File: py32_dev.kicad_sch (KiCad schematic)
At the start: 34 parts, among them J1 Board Pwr, J2 Conn_01x18, J3 Conn_01x18, SW1 Usr, SW2 Reset, U1 uA7805, U2 PY32F030K1xT, Y1 24MHz, Y2 32.768KHz

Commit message: Updated README
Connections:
- net GND: now also J2.1 (Pin_1); no longer J3.1 (Pin_1)
- net VDD: now also J3.1 (Pin_1); no longer J2.1 (Pin_1)
- net VBUS: now reaches C1.1, F1.1, J1.A9 (VBUS), J1.B9 (VBUS)
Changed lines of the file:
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@@
   (junction (at 57.15 60.96) (diameter 0) (color 0 0 0 0)
   )
+  (junction (at 207.01 33.02) (diameter 0) (color 0 0 0 0)
+  )
   (junction (at 62.865 123.825) (diameter 0) (color 0 0 0 0)
   )
@@
   (junction (at 47.625 116.205) (diameter 0) (color 0 0 0 0)
   )
-  (junction (at 243.84 33.02) (diameter 0) (color 0 0 0 0)
-  )
   (junction (at 47.625 131.445) (diameter 0) (color 0 0 0 0)
   )
@@
     (stroke (width 0) (type default) (color 0 0 0 0))
   )
-  (wire (pts (xy 233.045 24.765) (xy 243.84 24.765))
-    (stroke (width 0) (type default) (color 0 0 0 0))
-  )
   (wire (pts (xy 47.625 120.015) (xy 47.625 116.205))
     (stroke (width 0) (type default) (color 0 0 0 0))
   )
+  (wire (pts (xy 203.2 25.4) (xy 207.01 25.4))
+    (stroke (width 0) (type default) (color 0 0 0 0))
+  )
   (wire (pts (xy 47.625 89.535) (xy 47.625 94.615))
     (stroke (width 0) (type default) (color 0 0 0 0))
@@
     (stroke (width 0) (type default) (color 0 0 0 0))
   )
+  (wire (pts (xy 243.84 35.56) (xy 237.49 35.56))
+    (stroke (width 0) (type default) (color 0 0 0 0))
+  )
   (wire (pts (xy 66.675 60.96) (xy 66.675 58.42))
     (stroke (width 0) (type default) (color 0 0 0 0))
@@
     (stroke (width 0) (type default) (color 0 0 0 0))
   )
+  (wire (pts (xy 237.49 35.56) (xy 237.49 24.765))
+    (stroke (width 0) (type default) (color 0 0 0 0))
+  )
   (wire (pts (xy 57.15 60.96) (xy 66.675 60.96))
     (stroke (width 0) (type default) (color 0 0 0 0))
@@
     (stroke (width 0) (type default) (color 0 0 0 0))
   )
+  (wire (pts (xy 207.01 25.4) (xy 207.01 33.02))
+    (stroke (width 0) (type default) (color 0 0 0 0))
+  )
   (wire (pts (xy 89.535 189.865) (xy 89.535 194.31))
     (stroke (width 0) (type default) (color 0 0 0 0))
   )
+  (wire (pts (xy 237.49 24.765) (xy 233.045 24.765))
+    (stroke (width 0) (type default) (color 0 0 0 0))
+  )
   (wire (pts (xy 139.065 175.26) (xy 139.065 177.8))
     (stroke (width 0) (type default) (color 0 0 0 0))
@@
     (stroke (width 0) (type default) (color 0 0 0 0))
   )
+  (wire (pts (xy 207.01 33.02) (xy 207.01 35.56))
+    (stroke (width 0) (type default) (color 0 0 0 0))
+  )
   (wire (pts (xy 81.915 35.56) (xy 88.265 35.56))
     (stroke (width 0) (type default) (color 0 0 0 0))
   )
-  (wire (pts (xy 243.84 33.02) (xy 243.84 35.56))
-    (stroke (width 0) (type default) (color 0 0 0 0))
-  )
   (wire (pts (xy 66.675 48.26) (xy 66.675 50.8))
     (stroke (width 0) (type default) (color 0 0 0 0))
@@
     (stroke (width 0) (type default) (color 0 0 0 0))
   )
-  (wire (pts (xy 205.105 31.75) (xy 202.565 31.75))
-    (stroke (width 0) (type default) (color 0 0 0 0))
-  )
   (wire (pts (xy 234.95 130.175) (xy 237.49 130.175))
     (stroke (width 0) (type default) (color 0 0 0 0))
@@
     (stroke (width 0) (type default) (color 0 0 0 0))
   )
-  (wire (pts (xy 205.105 35.56) (xy 205.105 31.75))
-    (stroke (width 0) (type default) (color 0 0 0 0))
-  )
   (wire (pts (xy 207.645 140.97) (xy 217.805 140.97))
     (stroke (width 0) (type default) (color 0 0 0 0))
@@
     (stroke (width 0) (type default) (color 0 0 0 0))
   )
-  (wire (pts (xy 243.84 24.765) (xy 243.84 33.02))
-    (stroke (width 0) (type default) (color 0 0 0 0))
-  )
   (wire (pts (xy 52.705 48.26) (xy 66.675 48.26))
     (stroke (width 0) (type default) (color 0 0 0 0))
@@
   )
   (wire (pts (xy 40.005 116.205) (xy 47.625 116.205))
-    (stroke (width 0) (type default) (color 0 0 0 0))
-  )
-  (wire (pts (xy 207.01 35.56) (xy 205.105 35.56))
     (stroke (width 0) (type default) (color 0 0 0 0))
   )
@@
   )
   (text "PY32F030K18T6\nFlash 64k\nRam 8k" (at 93.98 136.525 0)
+    (effects (font (size 1.27 1.27)) (justify left bottom))
+  )
+  (label "VBUS" (at 53.975 35.56 0)
     (effects (font (size 1.27 1.27)) (justify left bottom))
   )
@@
     (pin "1")
   )
-  (symbol (lib_id "power:VDD") (at 207.01 33.02 0) (unit 1)
-    (in_bom yes) (on_board yes) (fields_autoplaced)
-    (property "Reference" "#PWR0125" (id 0) (at 207.01 36.83 0)
-      (effects (font (size 1.27 1.27)) hide)
-    )
-    (property "Value" "VDD" (id 1) (at 207.01 29.4442 0))
-    (property "Footprint" "" (id 2) (at 207.01 33.02 0)
-      (effects (font (size 1.27 1.27)) hide)
-    )
-    (property "Datasheet" "" (id 3) (at 207.01 33.02 0)
+  (symbol (lib_id "power:VDD") (at 243.84 33.02 0) (unit 1)
+    (in_bom yes) (on_board yes) (fields_autoplaced)
+    (property "Reference" "#PWR0125" (id 0) (at 243.84 36.83 0)
+      (effects (font (size 1.27 1.27)) hide)
+    )
+    (property "Value" "VDD" (id 1) (at 243.84 29.4442 0))
+    (property "Footprint" "" (id 2) (at 243.84 33.02 0)
+      (effects (font (size 1.27 1.27)) hide)
+    )
+    (property "Datasheet" "" (id 3) (at 243.84 33.02 0)
       (effects (font (size 1.27 1.27)) hide)
     )
@@
     (pin "2")
   )
-  (symbol (lib_id "power:GND") (at 202.565 31.75 0) (unit 1)
-    (in_bom yes) (on_board yes) (fields_autoplaced)
-    (property "Reference" "#PWR0126" (id 0) (at 202.565 38.1 0)
-      (effects (font (size 1.27 1.27)) hide)
-    )
-    (property "Value" "GND" (id 1) (at 202.565 36.1934 0))
-    (property "Footprint" "" (id 2) (at 202.565 31.75 0)
-      (effects (font (size 1.27 1.27)) hide)
-    )
-    (property "Datasheet" "" (id 3) (at 202.565 31.75 0)
-      (effects (font (size 1.27 1.27)) hide)
-    )
+  (symbol (lib_id "power:GND") (at 203.2 25.4 0) (unit 1)
+    (in_bom yes) (on_board yes) (fields_autoplaced)
+    (property "Reference" "#PWR0126" (id 0) (at 203.2 31.75 0)
+      (effects (font (size 1.27 1.27)) hide)
+    )
+    (property "Value" "GND" (id 1) (at 203.2 29.8434 0))
+    (property "Footprint" "" (id 2) (at 203.2 25.4 0)
+      (effects (font (size 1.27 1.27)) hide)
+    )
+    (property "Datasheet" "" (id 3) (at 203.2 25.4 0)
+      (effects (font (size 1.27 1.27)) hide)
+    )

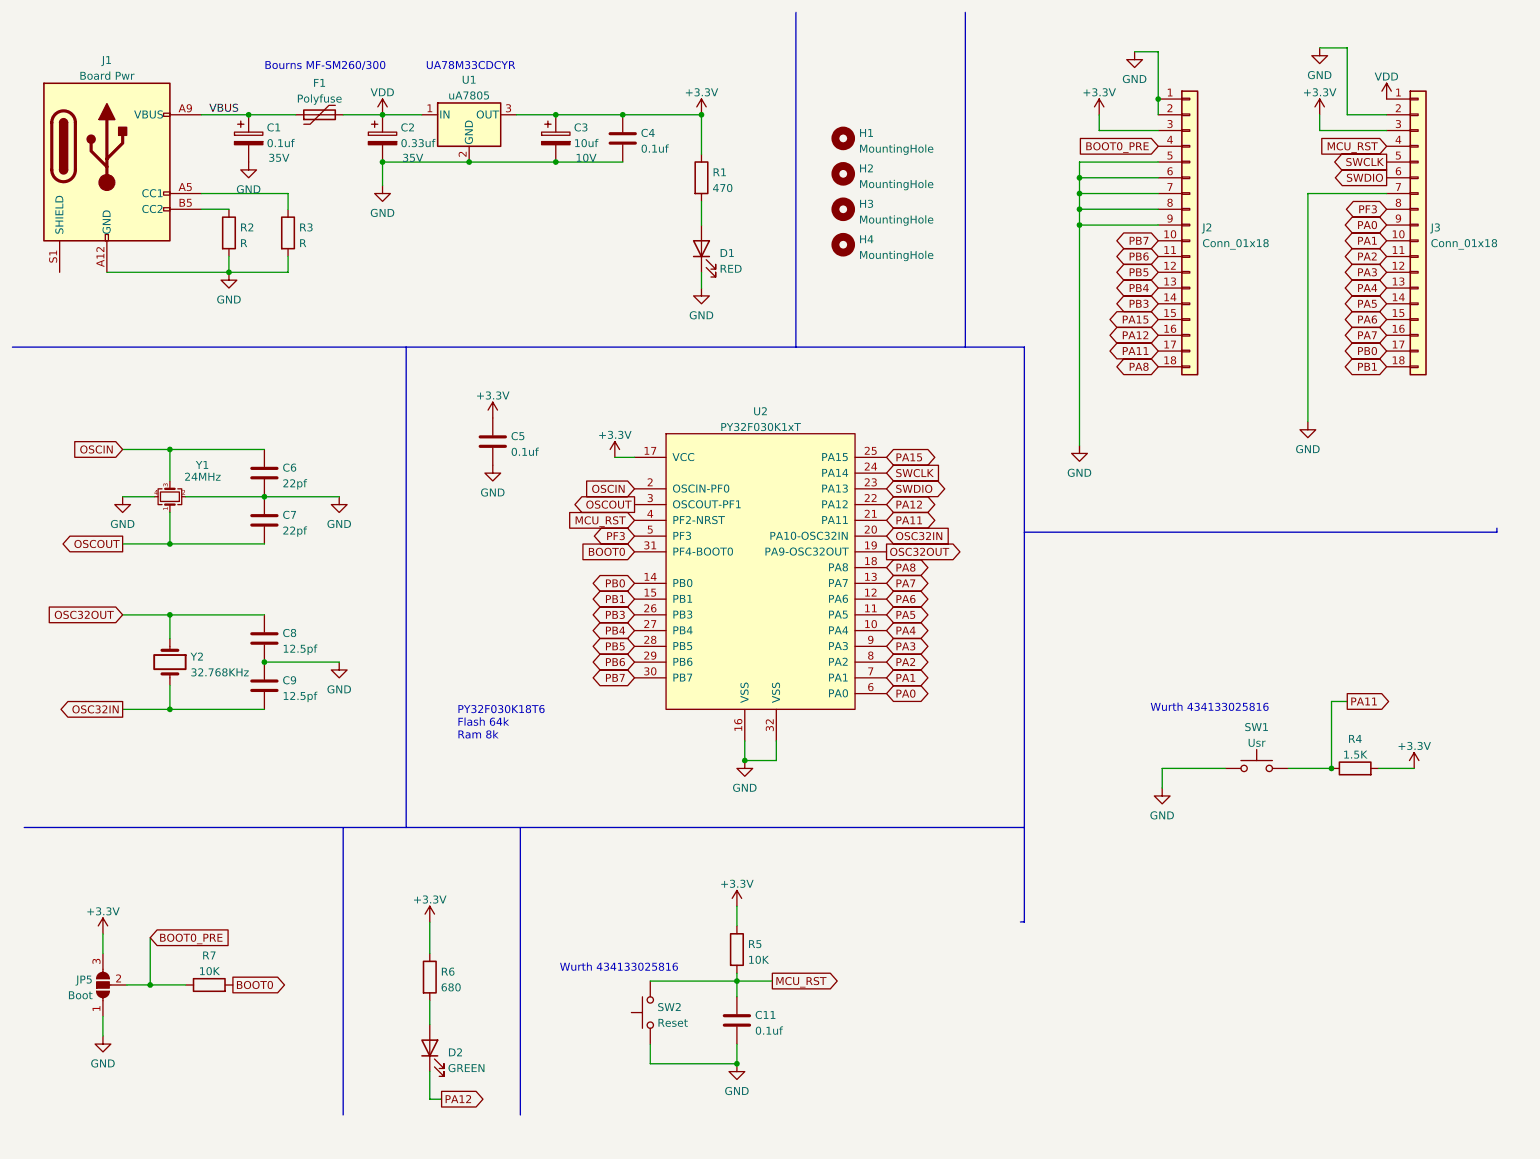
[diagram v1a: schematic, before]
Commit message: Added resistor values R2,R3
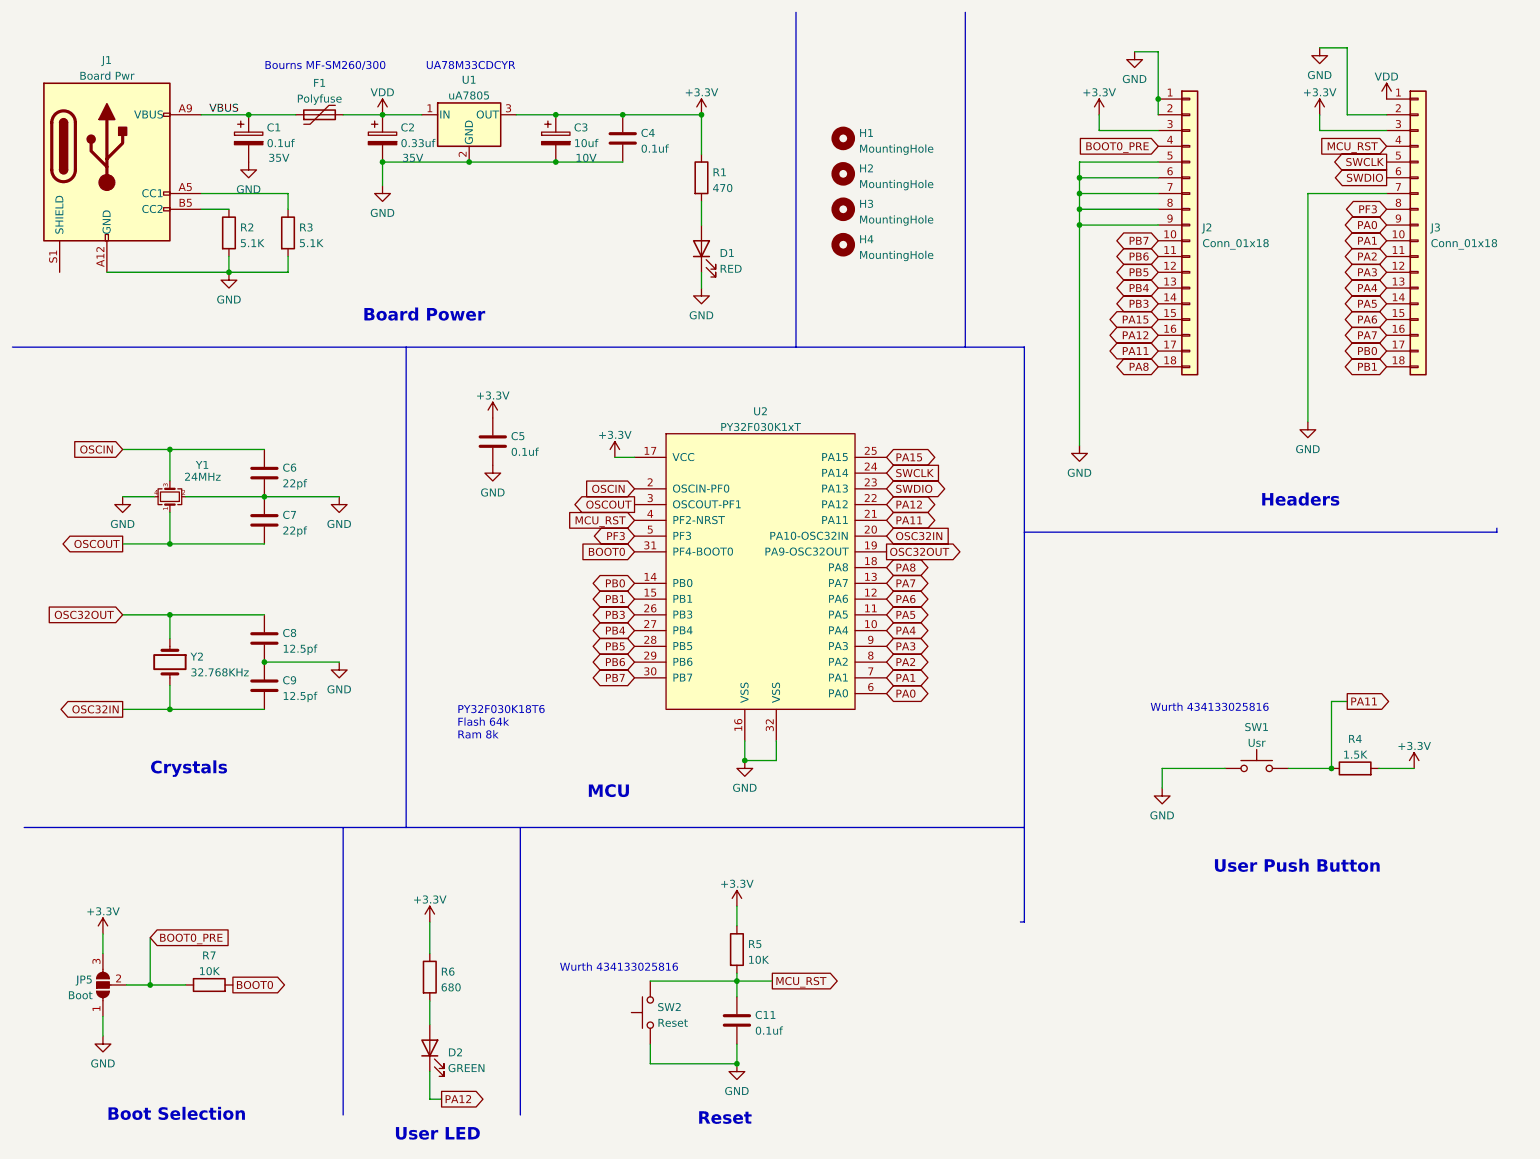
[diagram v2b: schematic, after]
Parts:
- R2, R3: value R -> 5.1K
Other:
- note added: "Board Power"
- note added: "Boot Selection"
- note added: "Crystals"
- note added: "Headers"
- note added: "MCU"
- note added: "Reset"
- note added: "User LED"
- note added: "User Push Button"
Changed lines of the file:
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@@
     (effects (font (size 1.27 1.27)) (justify left bottom))
+  )
+  (text "Headers" (at 223.52 99.06 0)
+    (effects (font (size 2 2) (thickness 0.4) bold) (justify left bottom))
+  )
+  (text "Boot Selection" (at 37.465 198.12 0)
+    (effects (font (size 2 2) (thickness 0.4) bold) (justify left bottom))
+  )
+  (text "Crystals" (at 44.45 142.24 0)
+    (effects (font (size 2 2) (thickness 0.4) bold) (justify left bottom))
+  )
+  (text "User Push Button" (at 215.9 158.115 0)
+    (effects (font (size 2 2) (thickness 0.4) bold) (justify left bottom))
+  )
+  (text "Reset" (at 132.715 198.755 0)
+    (effects (font (size 2 2) (thickness 0.4) bold) (justify left bottom))
   )
   (text "UA78M33CDCYR" (at 88.9 28.575 0)
     (effects (font (size 1.27 1.27)) (justify left bottom))
   )
+  (text "MCU" (at 114.935 146.05 0)
+    (effects (font (size 2 2) (thickness 0.4) bold) (justify left bottom))
+  )
   (text "Wurth 434133025816" (at 110.49 173.99 0)
     (effects (font (size 1.27 1.27)) (justify left bottom))
@@
     (effects (font (size 1.27 1.27)) (justify left bottom))
   )
+  (text "Board Power" (at 78.74 69.215 0)
+    (effects (font (size 2 2) (thickness 0.4) bold) (justify left bottom))
+  )
+  (text "User LED" (at 83.82 201.295 0)
+    (effects (font (size 2 2) (thickness 0.4) bold) (justify left bottom))
+  )
   (label "VBUS" (at 53.975 35.56 0)
     (effects (font (size 1.27 1.27)) (justify left bottom))
@@
       (effects (font (size 1.27 1.27)) (justify left))
     )
-    (property "Value" "R" (id 1) (at 68.453 56.3122 0)
+    (property "Value" "5.1K" (id 1) (at 68.453 56.3122 0)
       (effects (font (size 1.27 1.27)) (justify left))
     )
@@
       (effects (font (size 1.27 1.27)) (justify left))
     )
-    (property "Value" "R" (id 1) (at 58.928 56.3122 0)
+    (property "Value" "5.1K" (id 1) (at 58.928 56.3122 0)
       (effects (font (size 1.27 1.27)) (justify left))
     )
@@
     )
     (path "/df568ff5-b71f-4894-a2fc-e317e301e9f7"
-      (reference "R2") (unit 1) (value "R") (footprint "Resistor_SMD:R_0603_1608Metric")
+      (reference "R2") (unit 1) (value "5.1K") (footprint "Resistor_SMD:R_0603_1608Metric")
     )
     (path "/1c8480b2-49c3-4184-8576-974c02faadd0"
-      (reference "R3") (unit 1) (value "R") (footprint "Resistor_SMD:R_0603_1608Metric")
+      (reference "R3") (unit 1) (value "5.1K") (footprint "Resistor_SMD:R_0603_1608Metric")
     )
     (path "/cada5b00-0c0c-4001-beec-920de1988706"

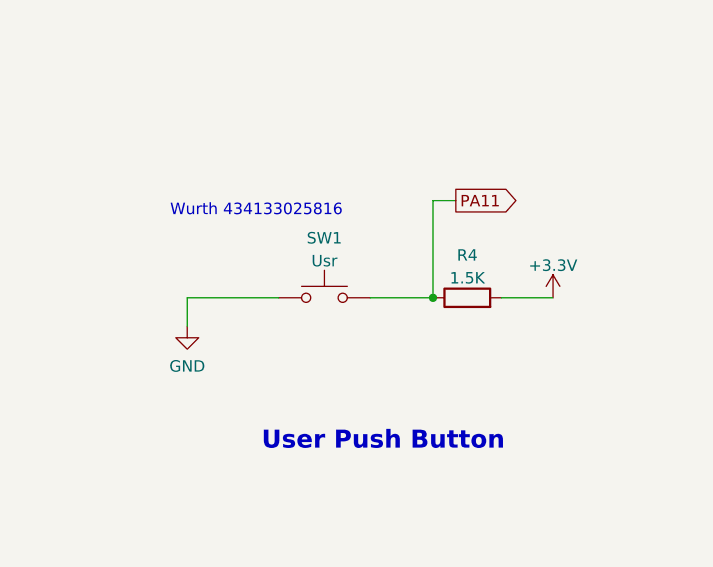
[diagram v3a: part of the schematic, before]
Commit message: Redid user pushbutton to work correctly
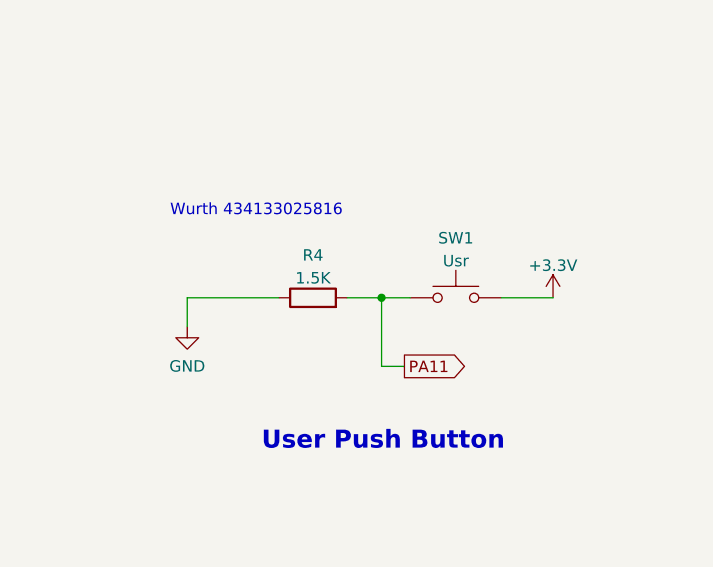
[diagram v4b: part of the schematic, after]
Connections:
- net +3.3V: now also SW1.2; no longer R4.2
- net GND: now also R4.1; no longer SW1.1
- net PA11: now also R4.2, SW1.1; no longer R4.1, SW1.2
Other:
- moved on the sheet: R4, SW1
